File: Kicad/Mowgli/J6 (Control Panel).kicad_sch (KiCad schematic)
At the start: 29 parts, among them J6 Control Panel, Q2 NMOS_G15, Q4 NMOS_G15, Q5 NMOS_G15, Q6 NMOS_G15, SW1 CLOCK, SW3 PLAY, U2 STM32F030R8T6, U3 AMS1117-3.3

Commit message: LED Labels ans some tiny stuff
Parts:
- added D?: LED, symbol Device:LED
- added R19, R24, R29, R32: 0, symbol Device:R
- added R?: 1k, symbol Device:R
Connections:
- net GND: now also D?.1 (K), R29.1, R32.1; no longer J6.12 (Pin_12), J6.13 (Pin_13), J6.15 (Pin_15), J6.7 (Pin_7), J6.8 (Pin_8)
- net J6_Pin_1: now also R19.2
- net J6_Pin_3: now also R24.2
- net at U2.14 (PA0): now also R?.2
- net at U2.16 (PA2): now also R19.1
- net at U2.17 (PA3): now also R24.1
- new net: J6.12 (Pin_12), J6.8 (Pin_8), R29.2
- new net: D?.2 (A), R?.1
- new net J6_Pin_15,13,12,8,7_GND: J6.13 (Pin_13), J6.15 (Pin_15), J6.7 (Pin_7), R32.2
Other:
- note added: "LED_2HR"
- note added: "LED_4HR"
- note added: "LED_6HR"
- note added: "LED_8HR"
- note added: "LED_BAT"
- note added: "LED_CHARGE"
- note added: "LED_FRI"
- note added: "LED_LIFTED"
- note added: "LED_LOCK"
- note added: "LED_MON"
- note added: "LED_PCB"
- note added: "LED_S1"
- note added: "LED_S2"
- note added: "LED_SAT"
- note added: "LED_SON"
- note added: "LED_THU"
- note added: "LED_TUE"
- note added: "LED_WED"
- note added: "LED_WIRE"
- note added: "U4_ESP_EN (Pin 2)"
- note added: "U4_ESP_IO0 (Pin 8)"
- note added: "U4_ESP_RST (Pin 15)"
- note added: "U4_ESP_RXD (Pin 11)"
- note added: "U4_ESP_TXD (Pin 12)"
- moved on the sheet: C3, C4, C5, C6, J6, R33, SW1, SW3, U3

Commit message: J6 and BTN changes
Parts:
- removed SW1: CLOCK, symbol Switch:SW_Push
- removed SW3: PLAY, symbol Switch:SW_Push
- added D22: NP, symbol Device:D
- added D? (x2): D, symbol Device:D
- added R20: 4k7, symbol Device:R
- added R25, R26, R28, R31, R37, R65, R66: 0, symbol Device:R
- added R34, R42, R57, R79: NP, symbol Device:R
- added R39, R52, R76: R0, symbol Device:R
- added R43: 10k, symbol Device:R
- added S10: BTN_WED, symbol Switch:SW_Push
- added S11: BTN_THU, symbol Switch:SW_Push
- added S3: BTN_PLAY, symbol Switch:SW_Push
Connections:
- net +3.3V: now also R20.1
- net GND: now also R43.1, S10.1, S11.1, S3.2
- net J6_Pin_14_Stop_yellow: now also R76.2; no longer Q5.3 (D), R74.2
- net J6_Pin_4_PLAY: now also R37.1
- net J6_Pin_6_Stop_white: now also R52.1; no longer Q2.3 (D), R50.2
- net at U2.25 (PC5): now also R57.2
- net at U2.27 (PB1): now also R28.2, R79.2
- net at U2.35 (PB14): now also D?.1 (K), S10.2
- net at U2.36 (PB15): now also D?.1 (K), S11.2
- net at U2.44 (PA11): now also R42.2
- net at U2.45 (PA12): now also R34.1
- net at U2.48 (PF7): now also R39.2
- net at U2.58 (PB6): now also R28.1, R66.1
- net at U2.59 (PB7): now also R31.1, R65.1
- net at U2.61 (PB8): now also R26.1
- net at U2.62 (PB9): now also R25.1
- net J6_Pin_2_CLOCK renamed J6_Pin_2_BTN-PullUp?
- net J6_Pin_2_BTN-PullUp?: now also D22.2 (A), D?.2 (A), D?.2 (A)
- new net: Q2.3 (D), R50.2, R52.2, R57.1
- new net: Q5.3 (D), R74.2, R76.1, R79.1
- new net: R20.2, R25.2
- new net: D22.1 (K), R37.2, R42.1, S3.1
- new net: R39.1, R43.2
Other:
- note added: "BTN_CLK (S1)"
- note added: "BTN_FRI (S12)"
- note added: "BTN_LOCK (S6)"
- note added: "BTN_MON (S8)"
- note added: "BTN_OK (S7)"
- note added: "BTN_S1 (S4)"
- note added: "BTN_S2 (S5)"
- note added: "BTN_SAT (S13)"
- note added: "BTN_SUN (S14)"
- note added: "BTN_TUE (S9)"
- note added: "Move R37 to R42 to get BTN_PLAY on GPIO PA11"
- note added: "The D seem to be on all Buttons (except "Play" which is NP)"
- note added: "U5-Pin1"
- note added: "U5-Pin10"
- note added: "U5-Pin2"
- note added: "U5-Pin3"
- note added: "U6 (Pin 2+3)"
- note added: "U7 Pin18"
- note added: "U7 Pin19"

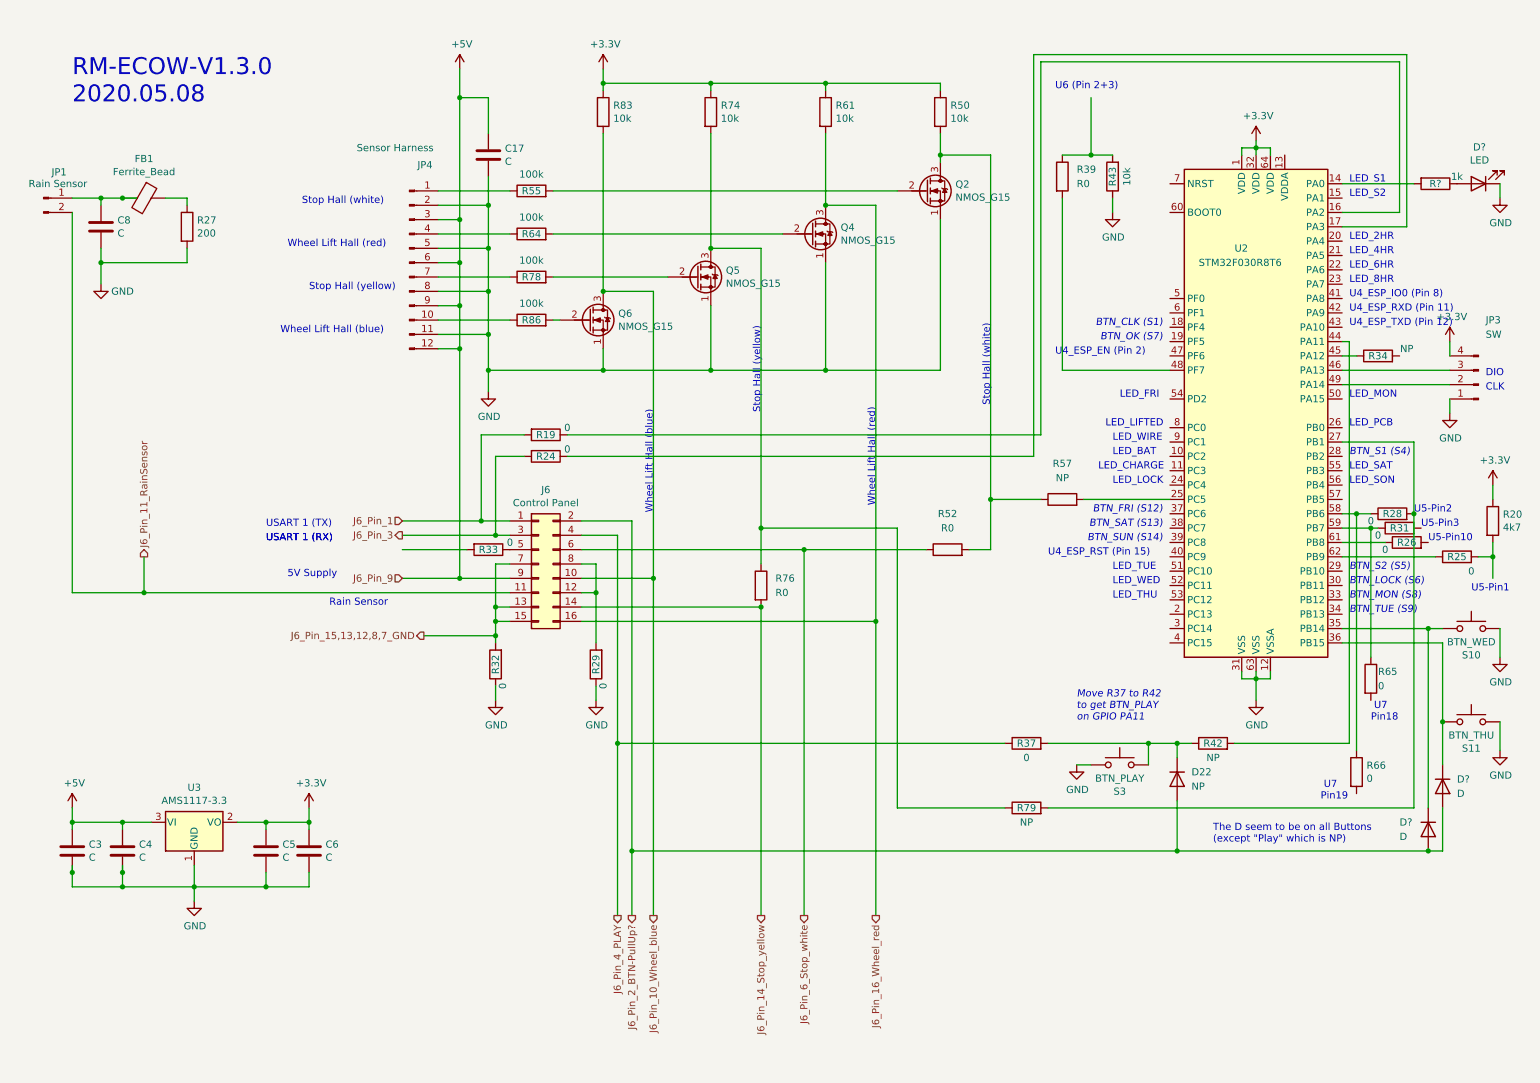
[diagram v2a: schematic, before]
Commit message: Remaining Buttons, in special Play & Home rerouting
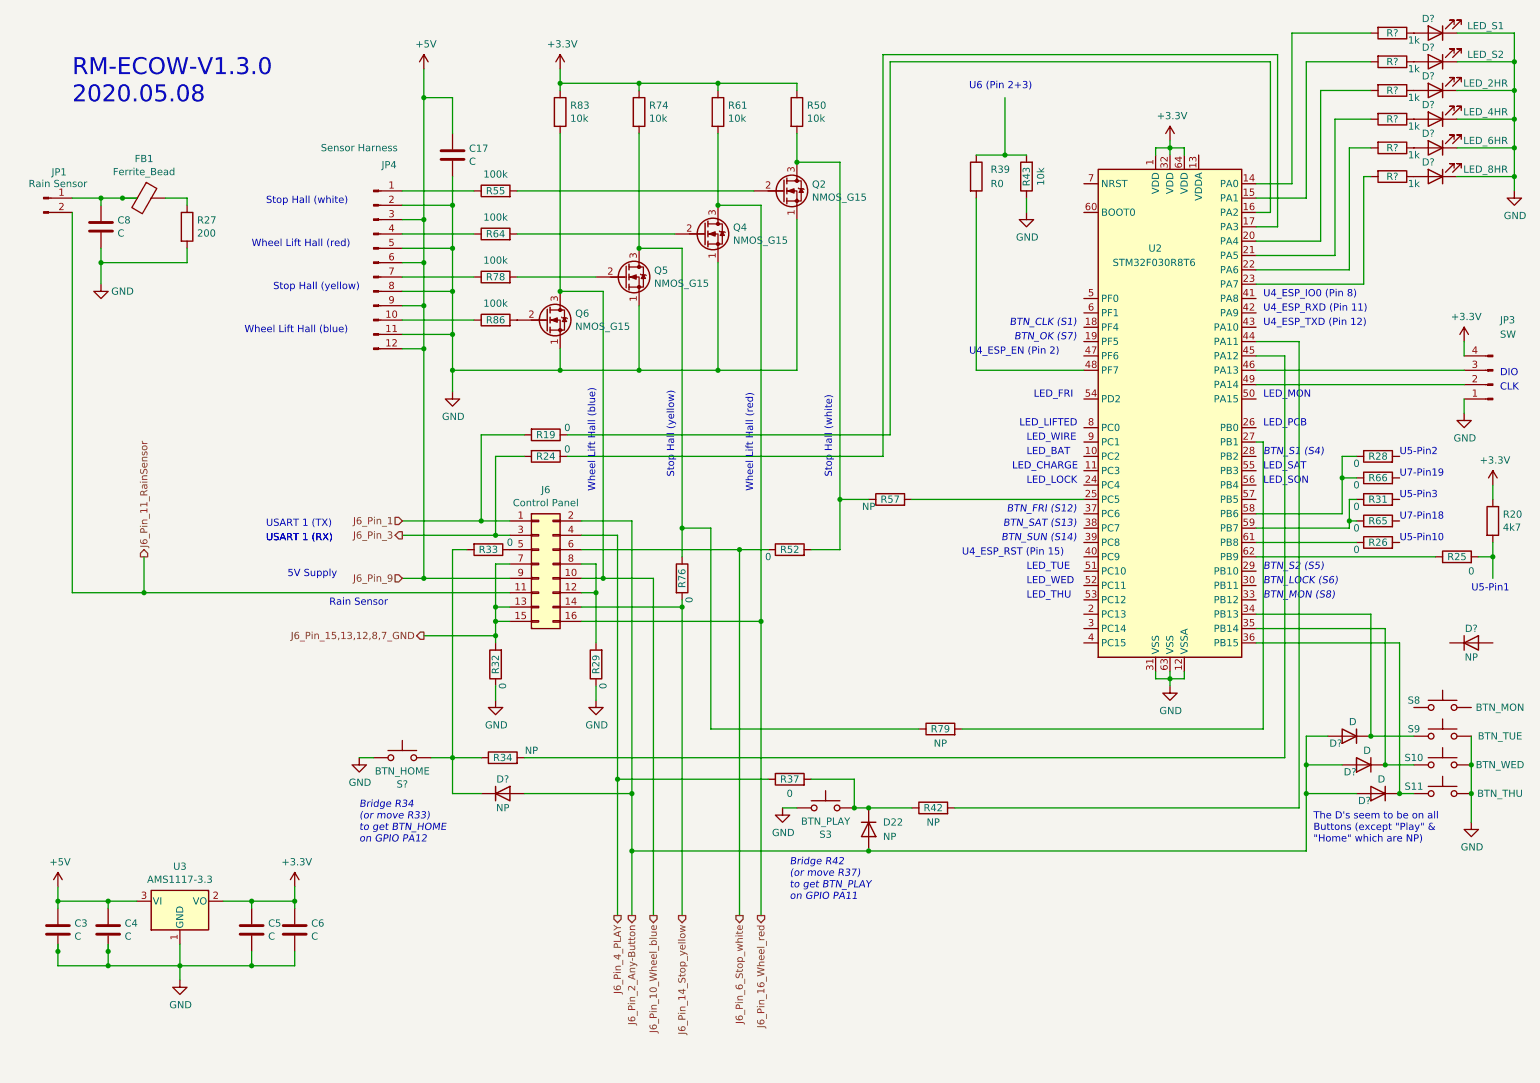
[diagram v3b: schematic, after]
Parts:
- removed D? (x2): D, symbol Device:D
- removed R66: 0, symbol Device:R
- added D? (x3): D, symbol Device:D
- added D?: LED_6HR, symbol Device:LED
- added D?: LED_S2, symbol Device:LED
- added D?: LED_8HR, symbol Device:LED
- added D?: LED_4HR, symbol Device:LED
- added D? (x2): NP, symbol Device:D
- added D?: LED_2HR, symbol Device:LED
- added R28: 0, symbol Device:R
- added R? (x5): 1k, symbol Device:R
- added S8: BTN_MON, symbol Switch:SW_Push
- added S9: BTN_TUE, symbol Switch:SW_Push
- added S?: BTN_HOME, symbol Switch:SW_Push
- D?: value LED -> LED_S1
- R52, R76: value R0 -> 0
- R65: now left out of the parts list
- renumbered R28 to R66
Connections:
- net GND: now also D?.1 (K), D?.1 (K), D?.1 (K), D?.1 (K), D?.1 (K), S9.1, S?.2
- net at R33.2: now also R34.1, D?.1 (K), S?.1
- net at S10.2, U2.35 (PB14): now also D?.1 (K)
- net at S11.2, U2.36 (PB15): now also D?.1 (K)
- net at U2.15 (PA1): now also R?.2
- net at U2.20 (PA4): now also R?.2
- net at U2.21 (PA5): now also R?.2
- net at U2.22 (PA6): now also R?.2
- net at U2.23 (PA7): now also R?.2
- net at R79.2, U2.27 (PB1): no longer R66.2
- net at U2.34 (PB13): now also D?.1 (K), S9.2
- net at U2.45 (PA12): now also R34.2; no longer R34.1
- net at R66.1, U2.58 (PB6): now also R28.1
- net J6_Pin_2_BTN-PullUp? renamed J6_Pin_2_Any-Button
- net J6_Pin_2_Any-Button: now also D?.2 (A), D?.2 (A), D?.2 (A), D?.2 (A)
- new net: D?.2 (A), R?.1 (x5)
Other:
- note added: "Bridge R34 (or move R33) to get BTN_HOME on GPIO PA12"
- note added: "Bridge R42 (or move R37) to get BTN_PLAY on GPIO PA11"
- note added: "The D's seem to be on all Buttons (except "Play" & "Home" which are NP)"
- note added: "U7-Pin18"
- note added: "U7-Pin19"
- note removed: "BTN_TUE (S9)"
- note removed: "LED_2HR"
- note removed: "LED_4HR"
- note removed: "LED_6HR"
- note removed: "LED_8HR"
- note removed: "LED_S1"
- note removed: "LED_S2"
- note removed: "Move R37 to R42 to get BTN_PLAY on GPIO PA11"
- note removed: "The D seem to be on all Buttons (except "Play" which is NP)"
- note removed: "U7 Pin18"
- note removed: "U7 Pin19"
- moved on the sheet: C17, C3, C4, C5, C6, D22, D?, JP3, JP4, Q2, Q4, Q5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

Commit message: Cleanup
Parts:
- removed R43: 10k, symbol Device:R
- added C2: ?, symbol Device:C
- added R5: NP, symbol Device:R
- added R?: 10k, symbol Device:R
- R39: value R0 -> 0; now left out of the parts list
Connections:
- net +3.3V: now also R5.2
- net GND: now also C2.2, R?.1
- net at U2.7 (NRST): now also C2.1, R5.1
- net at R39.1: now also R?.2
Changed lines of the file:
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@@
   (junction (at 140.97 26.67) (diameter 0) (color 0 0 0 0)
   )
-  (junction (at 191.77 39.37) (diameter 0) (color 0 0 0 0)
-  )
   (junction (at 256.54 142.24) (diameter 0) (color 0 0 0 0)
   )
@@
   (junction (at 88.9 58.42) (diameter 0) (color 0 0 0 0)
   )
+  (junction (at 191.77 44.45) (diameter 0) (color 0 0 0 0)
+  )
   (junction (at 167.64 154.94) (diameter 0) (color 0 0 0 0)
   )
@@
   (junction (at 58.42 171.45) (diameter 0) (color 0 0 0 0)
   )
+  (junction (at 179.07 77.47) (diameter 0) (color 0 0 0 0)
+  )
   (junction (at 140.97 48.26) (diameter 0) (color 0 0 0 0)
   )
@@
     (stroke (width 0) (type default) (color 0 0 0 0))
   )
+  (wire (pts (xy 191.77 44.45) (xy 205.74 44.45))
+    (stroke (width 0) (type default) (color 0 0 0 0))
+  )
   (wire (pts (xy 101.6 119.38) (xy 101.6 111.76))
     (stroke (width 0) (type default) (color 0 0 0 0))
@@
     (stroke (width 0) (type default) (color 0 0 0 0))
   )
-  (wire (pts (xy 191.77 39.37) (xy 195.58 39.37))
-    (stroke (width 0) (type default) (color 0 0 0 0))
-  )
   (wire (pts (xy 274.32 147.32) (xy 274.32 152.4))
     (stroke (width 0) (type default) (color 0 0 0 0))
@@
     (stroke (width 0) (type default) (color 0 0 0 0))
   )
-  (wire (pts (xy 186.69 46.99) (xy 186.69 77.47))
-    (stroke (width 0) (type default) (color 0 0 0 0))
-  )
   (wire (pts (xy 220.98 132.08) (xy 220.98 133.35))
     (stroke (width 0) (type default) (color 0 0 0 0))
@@
     (stroke (width 0) (type default) (color 0 0 0 0))
   )
+  (wire (pts (xy 179.07 60.96) (xy 179.07 77.47))
+    (stroke (width 0) (type default) (color 0 0 0 0))
+  )
   (wire (pts (xy 125.73 162.56) (xy 125.73 173.99))
     (stroke (width 0) (type default) (color 0 0 0 0))
@@
     (stroke (width 0) (type default) (color 0 0 0 0))
   )
-  (wire (pts (xy 186.69 77.47) (xy 205.74 77.47))
+  (wire (pts (xy 179.07 77.47) (xy 191.77 77.47))
     (stroke (width 0) (type default) (color 0 0 0 0))
   )
@@
     (stroke (width 0) (type default) (color 0 0 0 0))
   )
-  (wire (pts (xy 186.69 39.37) (xy 191.77 39.37))
-    (stroke (width 0) (type default) (color 0 0 0 0))
-  )
   (wire (pts (xy 104.14 119.38) (xy 101.6 119.38))
     (stroke (width 0) (type default) (color 0 0 0 0))
@@
     (stroke (width 0) (type default) (color 0 0 0 0))
   )
+  (wire (pts (xy 199.39 77.47) (xy 205.74 77.47))
+    (stroke (width 0) (type default) (color 0 0 0 0))
+  )
+  (wire (pts (xy 179.07 85.09) (xy 179.07 87.63))
+    (stroke (width 0) (type default) (color 0 0 0 0))
+  )
   (wire (pts (xy 88.9 73.66) (xy 88.9 66.04))
     (stroke (width 0) (type default) (color 0 0 0 0))
@@
     (stroke (width 0) (type default) (color 0 0 0 0))
   )
+  (wire (pts (xy 191.77 43.18) (xy 191.77 44.45))
+    (stroke (width 0) (type default) (color 0 0 0 0))
+  )
   (wire (pts (xy 275.59 110.49) (xy 278.13 110.49))
     (stroke (width 0) (type default) (color 0 0 0 0))
@@
     (stroke (width 0) (type default) (color 0 0 0 0))
   )
-  (wire (pts (xy 195.58 46.99) (xy 195.58 49.53))
-    (stroke (width 0) (type default) (color 0 0 0 0))
-  )
   (wire (pts (xy 236.22 107.95) (xy 254 107.95))
     (stroke (width 0) (type default) (color 0 0 0 0))
@@
     (stroke (width 0) (type default) (color 0 0 0 0))
   )
-  (wire (pts (xy 191.77 29.21) (xy 191.77 39.37))
-    (stroke (width 0) (type default) (color 0 0 0 0))
-  )
   (wire (pts (xy 254 92.71) (xy 251.46 92.71))
     (stroke (width 0) (type default) (color 0 0 0 0))
@@
     (effects (font (size 1.27 1.27)) (justify left bottom))
   )
-  (text "U6 (Pin 2+3)" (at 185.42 27.94 0)
+  (text "U6\n(Pin 2+3)" (at 173.99 59.69 0)
     (effects (font (size 1.27 1.27)) (justify left bottom))
   )
@@
     (pin "2")
   )
+  (symbol (lib_id "Device:R") (at 179.07 81.28 180) (unit 1)
+    (in_bom yes) (on_board yes)
+    (property "Reference" "R?" (id 0) (at 179.07 81.28 90))
+    (property "Value" "10k" (id 1) (at 181.61 81.28 90))
+    (property "Footprint" "" (id 2) (at 180.848 81.28 90)
+      (effects (font (size 1.27 1.27)) hide)
+    )
+    (property "Datasheet" "~" (id 3) (at 179.07 81.28 0)
+      (effects (font (size 1.27 1.27)) hide)
+    )
+    (pin "1")
+    (pin "2")
+  )
   (symbol (lib_id "Device:D") (at 255.27 147.32 180) (unit 1)
     (in_bom yes) (on_board yes)
@@
     (pin "2")
   )
+  (symbol (lib_id "Device:R") (at 191.77 39.37 180) (unit 1)
+    (in_bom yes) (on_board yes)
+    (property "Reference" "R5" (id 0) (at 191.77 39.37 90))
+    (property "Value" "NP" (id 1) (at 194.31 39.37 90))
+    (property "Footprint" "" (id 2) (at 193.548 39.37 90)
+      (effects (font (size 1.27 1.27)) hide)
+    )
+    (property "Datasheet" "~" (id 3) (at 191.77 39.37 0)
+      (effects (font (size 1.27 1.27)) hide)
+    )
+    (pin "1")
+    (pin "2")
+  )
   (symbol (lib_id "power:GND") (at 274.32 157.48 0) (unit 1)
     (in_bom yes) (on_board yes)
@@
     (pin "1")
     (pin "2")
+  )
+  (symbol (lib_id "Device:C") (at 191.77 48.26 0) (unit 1)
+    (in_bom yes) (on_board yes)
+    (property "Reference" "C2" (id 0) (at 194.691 47.0916 0)
+      (effects (font (size 1.27 1.27)) (justify left))
+    )
+    (property "Value" "?" (id 1) (at 194.691 49.403 0)
+      (effects (font (size 1.27 1.27)) (justify left))
+    )
+    (property "Footprint" "" (id 2) (at 192.7352 52.07 0)
+      (effects (font (size 1.27 1.27)) hide)
+    )
+    (property "Datasheet" "~" (id 3) (at 191.77 48.26 0)
+      (effects (font (size 1.27 1.27)) hide)
+    )
+    (pin "1")
+    (pin "2")
+  )
+  (symbol (lib_id "power:+3.3V") (at 191.77 35.56 0) (unit 1)
+    (in_bom yes) (on_board yes)
+    (property "Reference" "#PWR?" (id 0) (at 191.77 39.37 0)
+      (effects (font (size 1.27 1.27)) hide)
+    )
+    (property "Value" "+3.3V" (id 1) (at 192.151 31.1658 0))
+    (property "Footprint" "" (id 2) (at 191.77 35.56 0)
+      (effects (font (size 1.27 1.27)) hide)
+    )
+    (property "Datasheet" "" (id 3) (at 191.77 35.56 0)
+      (effects (font (size 1.27 1.27)) hide)
+    )
+    (pin "1")
   )
   (symbol (lib_id "Device:R") (at 257.81 92.71 90) (unit 1)
@@
     )
     (property "Datasheet" "" (id 3) (at 281.94 45.72 0)
+      (effects (font (size 1.27 1.27)) hide)
+    )
+    (pin "1")
+  )
+  (symbol (lib_id "power:GND") (at 191.77 52.07 0) (unit 1)
+    (in_bom yes) (on_board yes)
+    (property "Reference" "#PWR?" (id 0) (at 191.77 58.42 0)
+      (effects (font (size 1.27 1.27)) hide)
+    )
+    (property "Value" "GND" (id 1) (at 191.897 56.4642 0))
+    (property "Footprint" "" (id 2) (at 191.77 52.07 0)
+      (effects (font (size 1.27 1.27)) hide)
+    )
+    (property "Datasheet" "" (id 3) (at 191.77 52.07 0)
       (effects (font (size 1.27 1.27)) hide)
     )
@@
     (pin "2")
   )
+  (symbol (lib_id "power:GND") (at 179.07 87.63 0) (unit 1)
+    (in_bom yes) (on_board yes)
+    (property "Reference" "#PWR?" (id 0) (at 179.07 93.98 0)
+      (effects (font (size 1.27 1.27)) hide)
+    )
+    (property "Value" "GND" (id 1) (at 179.197 92.0242 0))
+    (property "Footprint" "" (id 2) (at 179.07 87.63 0)
+      (effects (font (size 1.27 1.27)) hide)
+    )
+    (property "Datasheet" "" (id 3) (at 179.07 87.63 0)
+      (effects (font (size 1.27 1.27)) hide)
+    )
+    (pin "1")
+  )
   (symbol (lib_id "Device:R") (at 260.35 38.1 270) (unit 1)
     (in_bom yes) (on_board yes)
@@
     (pin "2")
   )
-  (symbol (lib_id "power:GND") (at 195.58 49.53 0) (unit 1)
-    (in_bom yes) (on_board yes)
-    (property "Reference" "#PWR?" (id 0) (at 195.58 55.88 0)
-      (effects (font (size 1.27 1.27)) hide)
-    )
-    (property "Value" "GND" (id 1) (at 195.707 53.9242 0))
-    (property "Footprint" "" (id 2) (at 195.58 49.53 0)
-      (effects (font (size 1.27 1.27)) hide)
-    )
-    (property "Datasheet" "" (id 3) (at 195.58 49.53 0)
-      (effects (font (size 1.27 1.27)) hide)
-    )
-    (pin "1")
-  )
-  (symbol (lib_id "Device:R") (at 195.58 43.18 180) (unit 1)
-    (in_bom yes) (on_board yes)
-    (property "Reference" "R43" (id 0) (at 195.58 43.18 90))
-    (property "Value" "10k" (id 1) (at 198.12 43.18 90))
-    (property "Footprint" "" (id 2) (at 197.358 43.18 90)
-      (effects (font (size 1.27 1.27)) hide)
-    )
-    (property "Datasheet" "~" (id 3) (at 195.58 43.18 0)
-      (effects (font (size 1.27 1.27)) hide)
-    )
-    (pin "1")
-    (pin "2")
-  )
   (symbol (lib_id "Device:LED") (at 267.97 27.94 180) (unit 1)
     (in_bom yes) (on_board yes)
@@
     )
     (property "Datasheet" "~" (id 3) (at 267.97 27.94 0)
-      (effects (font (size 1.27 1.27)) hide)
-    )
-    (pin "1")
-    (pin "2")
-  )
-  (symbol (lib_id "Device:R") (at 186.69 43.18 0) (unit 1)
-    (in_bom yes) (on_board yes) (fields_autoplaced)
-    (property "Reference" "R39" (id 0) (at 189.23 41.9099 0)
-      (effects (font (size 1.27 1.27)) (justify left))
-    )
-    (property "Value" "R0" (id 1) (at 189.23 44.4499 0)
-      (effects (font (size 1.27 1.27)) (justify left))
-    )
-    (property "Footprint" "" (id 2) (at 184.912 43.18 90)
-      (effects (font (size 1.27 1.27)) hide)
-    )
-    (property "Datasheet" "~" (id 3) (at 186.69 43.18 0)
       (effects (font (size 1.27 1.27)) hide)
     )
@@
       (effects (font (size 1.27 1.27)) hide)
     )
+    (pin "1")
+    (pin "2")
+  )
+  (symbol (lib_id "Device:R") (at 195.58 77.47 90) (unit 1)
+    (in_bom no) (on_board no)
+    (property "Reference" "R39" (id 0) (at 195.58 77.47 90))
+    (property "Value" "0" (id 1) (at 199.39 78.74 90))
+    (property "Footprint" "" (id 2) (at 195.58 79.248 90)
+      (effects (font (size 1.27 1.27)) hide)
+    )
+    (property "Datasheet" "~" (id 3) (at 195.58 77.47 0)
+      (effects (font (size 1.27 1.27)) hide)
+    )
